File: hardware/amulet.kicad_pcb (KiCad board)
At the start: 2 copper layers, 21 x 21 mm, 22 parts, among them U1 ATtiny84A-MMH, U2 TTP223-BA6, U3 VEML6075

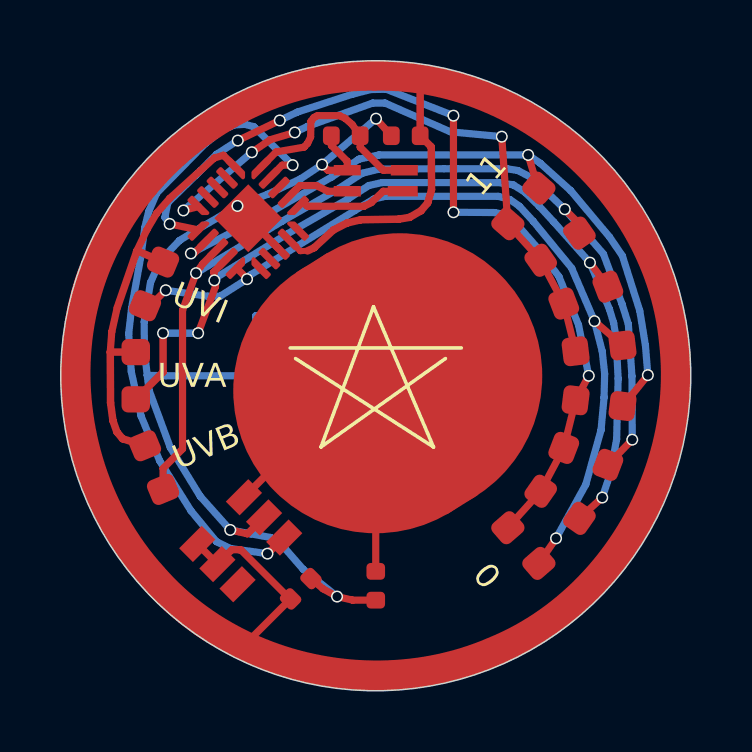
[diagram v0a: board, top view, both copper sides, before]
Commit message: Add programming test points
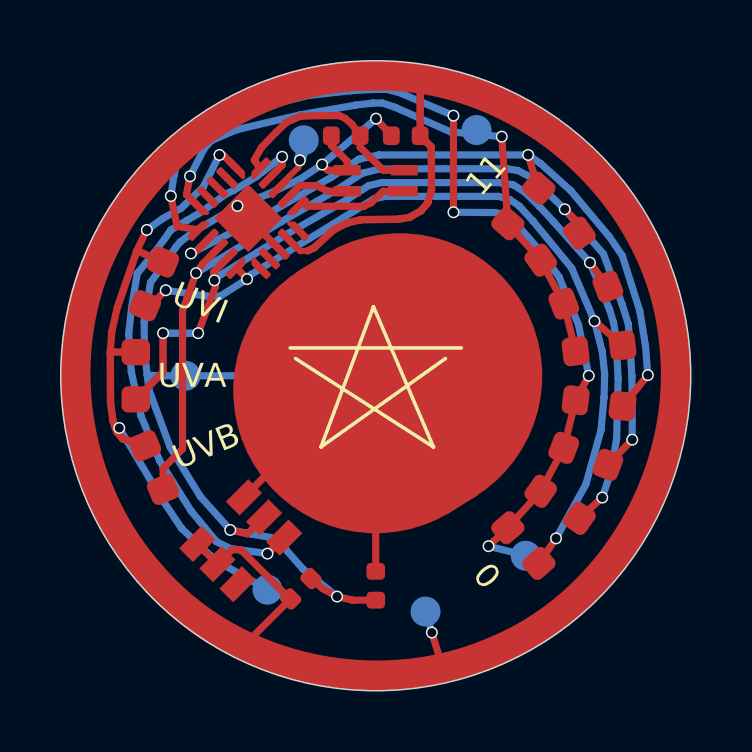
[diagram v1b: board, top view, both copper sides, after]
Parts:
- added TP4: RST, TestPoint:TestPoint_Pad_D1.0mm, B.Cu at (97.6, 92.2)
- added TP5: GND, TestPoint:TestPoint_Pad_D1.0mm, B.Cu at (93.7, 100.0)
- added TP6: VDD, TestPoint:TestPoint_Pad_D1.0mm, B.Cu at (101.7, 107.9)
- added TP7: SCK, TestPoint:TestPoint_Pad_D1.0mm, B.Cu at (105.0, 106.0)
- added TP8: MISO, TestPoint:TestPoint_Pad_D1.0mm, B.Cu at (103.4, 91.8)
- added TP9: MOSI, TestPoint:TestPoint_Pad_D1.0mm, B.Cu at (96.4, 107.1)
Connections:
- net Net-(D1-Pad1) renamed /PA4
- net Net-(D10-Pad1) renamed /PA6
- net Net-(D5-Pad1) renamed /PA5
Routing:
- net GND: track 70.8 -> 38.8 mm
- net VDD: track 44.2 -> 52.7 mm, vias 0 -> 1
- net /PA6: track 14.1 -> 21.8 mm, vias 0 -> 3
- net /PA4: track 29.6 -> 32.2 mm, vias 6 -> 5
- net /BUTTON: track 21.9 -> 19.4 mm
- net Net-(TP4-Pad1): track 0.00 -> 1.84 mm, vias 0 -> 1
- net /PA5: track 20.2 -> 20.6 mm, vias 4 -> 2

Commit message: Add UV star and graph markers
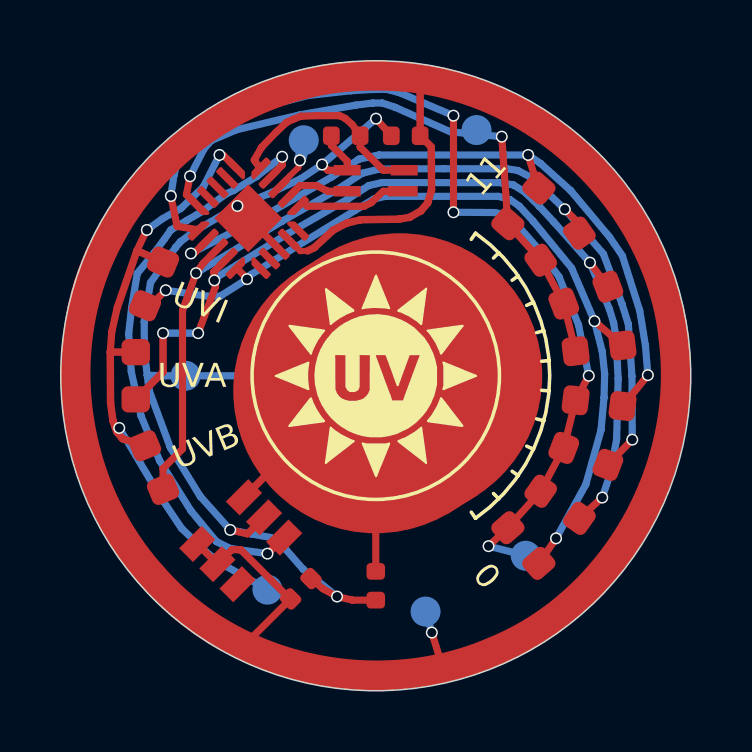
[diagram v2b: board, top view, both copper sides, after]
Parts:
- added svg2mod: G***, amulet:uvstar1, F.Cu at (95.3, 95.2)

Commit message: Final fixes
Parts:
- added REF**: PinHeader_1x01_P1.00mm_Horizontal, Connector_PinHeader_1.00mm:PinHeader_1x01_P1.00mm_Horizontal, F.Cu at (90.0, 100.0)
- added REF**: PinHeader_1x01_P1.00mm_Horizontal, Connector_PinHeader_1.00mm:PinHeader_1x01_P1.00mm_Horizontal, F.Cu at (110.0, 100.0)
- moved C4 1.73 mm to (98.6, 108.0), turned to 60 degrees
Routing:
- net VDD: track 52.7 -> 67.2 mm
- net /CapSense: track 9.90 -> 15.6 mm
- net GND: track 38.8 -> 38.0 mm
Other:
- board text added: "2 0 2 1"
- board text added: "M I T X E L A"
